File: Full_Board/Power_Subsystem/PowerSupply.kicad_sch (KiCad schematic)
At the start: 10 parts, among them J1 KLDHCX-8-0202-A, U1 LM2576SX-3.3/NOPB

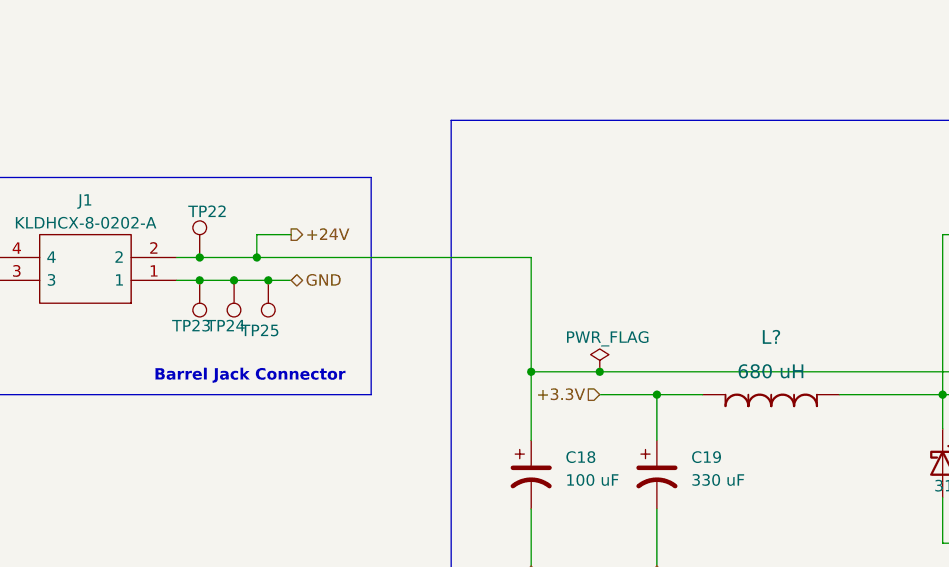
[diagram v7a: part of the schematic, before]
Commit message: Switched the pins on the barrel jack connector
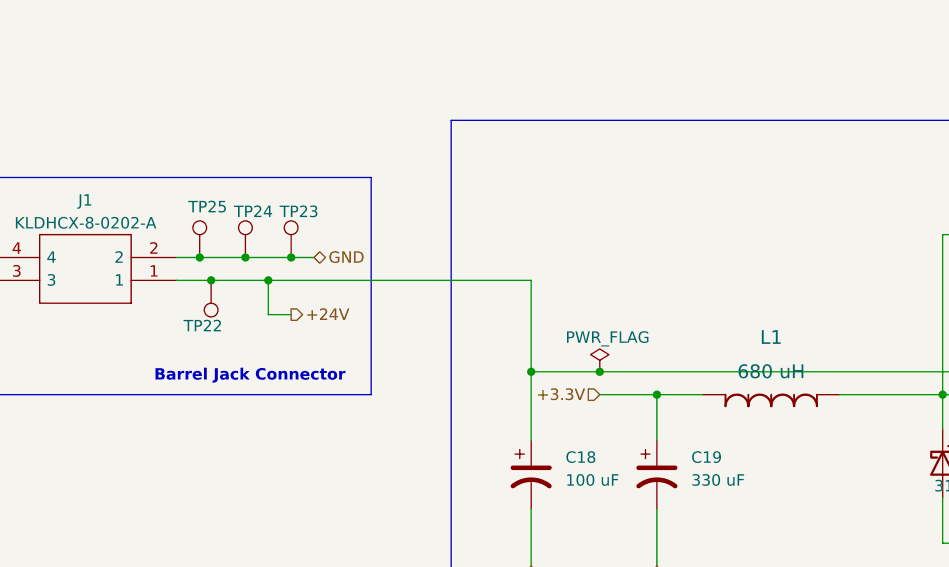
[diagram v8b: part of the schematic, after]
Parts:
- J1: footprint Power_Connector_KLDHCX:KLDHCX80202A -> KLDHCX80202A; Digikey link https://www.digikey.in/en/products/detail/kycon-inc/KLDHCX-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 -> https://www.digikey.com/en/products/detail/kycon-inc/KLDHCX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
- gave numbers to parts that had none: 1
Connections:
- net +24V: now also J1.1; no longer J1.2
- net GND: now also J1.2; no longer J1.1
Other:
- moved on the sheet: TP22, TP23, TP24, TP25
